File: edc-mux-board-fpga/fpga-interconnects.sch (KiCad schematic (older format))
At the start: 20 parts, among them J5 FPGA_JTAG, U6 10CL040YF484I7G, U63 S25FL128L

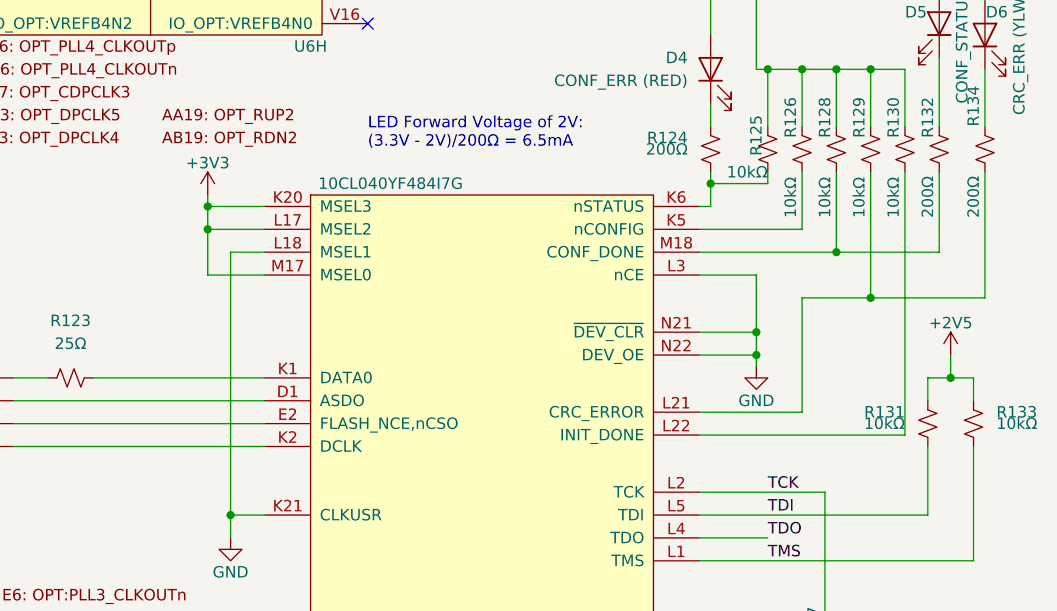
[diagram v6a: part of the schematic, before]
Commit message: Added labels to nets
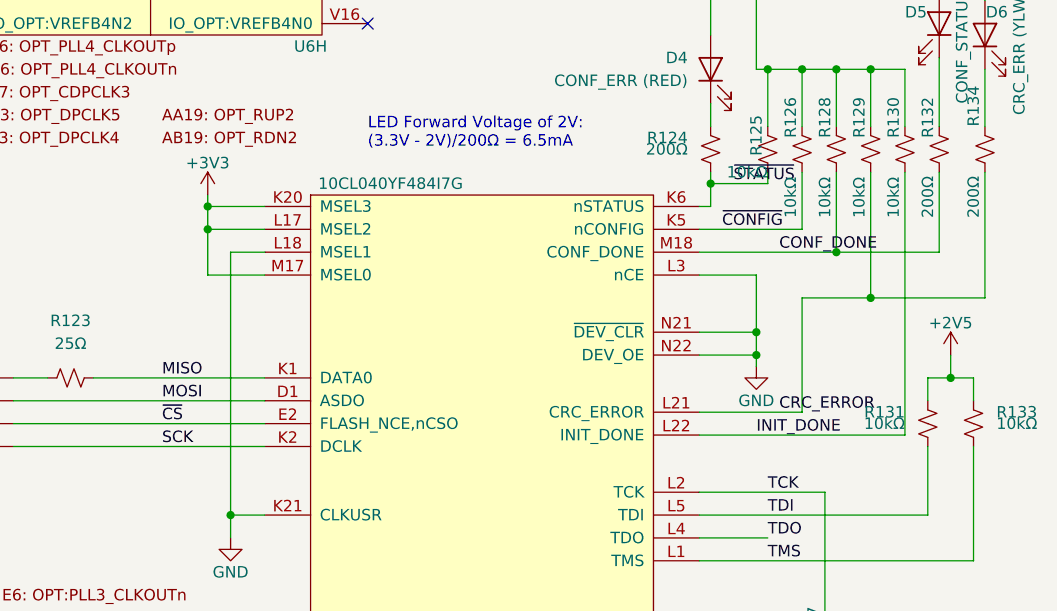
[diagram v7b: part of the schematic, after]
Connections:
- net MOSI: now reaches U6.D1 (ASDO), U63.5 (MOSI)
- net ~CS: now reaches U6.E2 (FLASH_NCE,nCSO), U63.1 (~CS)
- net MISO: now reaches R123.1, U6.K1 (DATA0)
- net SCK: now reaches U6.K2 (DCLK), U63.6 (SCK)
- net ~CONFIG: now reaches R126.1, U6.K5 (nCONFIG)
- net ~STATUS: now reaches R124.1, R125.1, U6.K6 (nSTATUS)
- net CRC_ERROR: now reaches R129.1, R134.2, U6.L21 (CRC_ERROR)
- net INIT_DONE: now reaches R130.1, U6.L22 (INIT_DONE)
- net CONF_DONE: now reaches R128.1, R132.1, U6.M18 (CONF_DONE)
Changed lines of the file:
@@
 Wire Bus Line
 	7100 1450 7100 3500
+Text Label 15250 5150 0    50   ~ 0
+INIT_DONE
+Text Label 15350 5050 0    50   ~ 0
+CRC_ERROR
+Text Label 15350 4350 0    50   ~ 0
+CONF_DONE
+Text Label 15100 4250 0    50   ~ 0
+~CONFIG
+Text Label 15150 4050 0    50   ~ 0
+~STATUS
+Text Label 12650 4900 0    50   ~ 0
+MISO
+Text Label 12650 5000 0    50   ~ 0
+MOSI
+Text Label 12650 5100 0    50   ~ 0
+~CS
+Text Label 12650 5200 0    50   ~ 0
+SCK
 $EndSCHEMATC

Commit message: updating FPGA pin assignments in schematic
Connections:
- wire segments 221 -> 234
- no-connect marks 203 -> 201
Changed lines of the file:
@@
 $Descr USLedger 17000 11000
 encoding utf-8
-Sheet 24 28
+Sheet 28 28
 Title ""
 Date ""
@@
 	1    0    0    -1
 $EndComp
+Text Label 8000 3100 2    50   ~ 0
+BCLK0
+Text Label 8000 3300 2    50   ~ 0
+WCLK0
 Text Label 8000 3000 2    50   ~ 0
-BCLK0
-Text Label 8000 2900 2    50   ~ 0
-WCLK0
-Text Label 8000 3300 2    50   ~ 0
 DOUT0
-Text Label 8000 3100 2    50   ~ 0
-DIN0
+Text Label 10150 1900 0    50   ~ 0
+BCLK1
+Text Label 10150 2000 0    50   ~ 0
+WCLK1
 Text Label 10150 1400 0    50   ~ 0
-BCLK1
+DOUT1
 Text Label 10150 1300 0    50   ~ 0
-WCLK1
-Text Label 10150 2000 0    50   ~ 0
-DOUT1
-Text Label 10150 1900 0    50   ~ 0
 DIN1
-Text Label 11500 1950 2    50   ~ 0
-BCLK4
-Text Label 10150 2100 0    50   ~ 0
+Text Label 10150 2800 0    50   ~ 0
 WCLK2
 Text Label 11500 1350 2    50   ~ 0
@@
 Text Label 11500 1250 2    50   ~ 0
 DIN3
-Text Label 1850 5350 2    50   ~ 0
-BCLK3
-Text Label 1850 5450 2    50   ~ 0
-WCLK3
 $Comp
 L SW-Intel:10CL040YF484I7G U?
@@
 	1    0    0    -1
 $EndComp
+Text Label 10150 2700 0    50   ~ 0
+BCLK2
 Text Label 10150 2200 0    50   ~ 0
-BCLK2
-Text Label 11500 1850 2    50   ~ 0
-WCLK4
-Text Label 10150 2800 0    50   ~ 0
 DOUT2
-Text Label 10150 2700 0    50   ~ 0
+Text Label 10150 2100 0    50   ~ 0
 DIN2
 $Comp
@@
 NoConn ~ 10050 2600
 NoConn ~ 10050 3300
-Wire Wire Line
-	1850 5350 2250 5350
-Wire Wire Line
-	1850 5450 2250 5450
+Text Label 13700 1450 0    50   ~ 0
+WCLK5
+Text Label 11500 1850 2    50   ~ 0
+DIN4
 Text Label 13700 1150 0    50   ~ 0
-WCLK5
-Text Label 11500 2250 2    50   ~ 0
-DIN4
-Text Label 13700 1350 0    50   ~ 0
 DIN5
-Text Label 11500 2350 2    50   ~ 0
+Text Label 11500 1950 2    50   ~ 0
 DOUT4
-Text Label 13700 1450 0    50   ~ 0
+Text Label 13700 1250 0    50   ~ 0
 DOUT5
 Text Label 11500 1650 2    50   ~ 0
@@
 Text Label 11500 3050 2    50   ~ 0
 DEV_ATT5
-Text Label 13700 1250 0    50   ~ 0
+Text Label 13700 1350 0    50   ~ 0
 BCLK5
 Wire Wire Line
@@
 Wire Wire Line
 	11500 1650 11650 1650
-Wire Wire Line
-	11500 1850 11650 1850
-Wire Wire Line
-	11500 1950 11650 1950
 Wire Wire Line
 	11500 2250 11650 2250
@@
 	13550 1550 13700 1550
 NoConn ~ 11650 1150
-NoConn ~ 11650 1450
-NoConn ~ 11650 1550
 NoConn ~ 11650 1750
 NoConn ~ 11650 2050
@@
 NoConn ~ 13550 2850
 NoConn ~ 13550 3350
+Text Label 3200 7450 0    50   ~ 0
+BCLK6
+Text Label 3200 7650 0    50   ~ 0
+WCLK6
 Text Label 3200 7850 0    50   ~ 0
-BCLK6
+DOUT6
 Text Label 3200 7750 0    50   ~ 0
-WCLK6
-Text Label 3200 7650 0    50   ~ 0
-DOUT6
-Text Label 3200 7450 0    50   ~ 0
 DIN6
 Text Label 3200 7150 0    50   ~ 0
@@
 Text Label 3200 7050 0    50   ~ 0
 DEV_ATT6
+Text Label 1000 8250 2    50   ~ 0
+WCLK7
 Text Label 3200 6650 0    50   ~ 0
-WCLK7
-Text Label 1000 8050 2    50   ~ 0
 DIN7
-Text Label 1000 8250 2    50   ~ 0
+Text Label 3200 6750 0    50   ~ 0
 DOUT7
 Text Label 1850 4850 2    50   ~ 0
@@
 Wire Wire Line
 	1850 4850 2250 4850
-Text Label 3200 6750 0    50   ~ 0
+Text Label 1000 8050 2    50   ~ 0
 BCLK7
 Wire Wire Line
+	3050 7450 3200 7450
+Wire Wire Line
+	3050 7650 3200 7650
+Wire Wire Line
+	3050 6650 3200 6650
+Wire Wire Line
+	3050 6750 3200 6750
+Wire Wire Line
+	3050 7050 3200 7050
+Wire Wire Line
+	3050 7150 3200 7150
+Wire Wire Line
 	1000 8050 1150 8050
 Wire Wire Line
 	1000 8250 1150 8250
-Wire Wire Line
-	3050 6650 3200 6650
-Wire Wire Line
-	3050 6750 3200 6750
-Wire Wire Line
-	3050 7050 3200 7050
-Wire Wire Line
-	3050 7150 3200 7150
-Wire Wire Line
-	3050 7450 3200 7450
-Wire Wire Line
-	3050 7650 3200 7650
 Wire Wire Line
 	3050 7750 3200 7750
@@
 Text Label 4250 7550 2    50   ~ 0
 BCLK9
+Text Label 6450 6950 0    50   ~ 0
+DOUT8
+Text Label 6450 6750 0    50   ~ 0
+DIN8
 Text Label 6450 6450 0    50   ~ 0
-DOUT8
+DEV_INT8
 Text Label 6450 6350 0    50   ~ 0
-DIN8
-Text Label 4250 8050 2    50   ~ 0
-DEV_INT8
-Text Label 4250 7950 2    50   ~ 0
 DEV_ATT8
 NoConn ~ 1150 6350
@@
 Text Label 4250 7650 2    50   ~ 0
 WCLK9
-Text Label 4250 6850 2    50   ~ 0
+Text Label 4250 7950 2    50   ~ 0
 DIN9
-Text Label 4250 7050 2    50   ~ 0
+Text Label 4250 8050 2    50   ~ 0
 DOUT9
-Text Label 4250 6750 2    50   ~ 0
-DEV_INT9
-Text Label 4250 6650 2    50   ~ 0
-DEV_ATT9
-Wire Wire Line
-	4250 6650 4400 6650
-Wire Wire Line
-	4250 6750 4400 6750
 Wire Wire Line
 	4250 6850 4400 6850
@@
 	4250 7050 4400 7050
 Wire Wire Line
+	4250 7950 4400 7950
+Wire Wire Line
+	4250 8050 4400 8050
+Wire Wire Line
 	4250 7550 4400 7550
 Wire Wire Line
 	4250 7650 4400 7650
 Wire Wire Line
-	4250 7950 4400 7950
-Wire Wire Line
-	4250 8050 4400 8050
-Wire Wire Line
-	6300 6350 6450 6350
-Wire Wire Line
-	6300 6450 6450 6450
+	6450 6350 6300 6350
+Wire Wire Line
+	6450 6450 6300 6450
+Wire Wire Line
+	6300 6750 6450 6750
+Wire Wire Line
+	6300 6950 6450 6950
 $Comp
 L SW-Intel:10CL040YF484I7G U6
@@
 NoConn ~ 6300 6550
 NoConn ~ 6300 6650
-NoConn ~ 6300 6750
-NoConn ~ 6300 6950
 NoConn ~ 6300 7050
 NoConn ~ 6300 7150
 NoConn ~ 6300 7250
 NoConn ~ 6300 8450
+Text Label 7350 7050 2    50   ~ 0
+BCLK10
+Text Label 7350 7250 2    50   ~ 0
+WCLK10
 Text Label 7350 7650 2    50   ~ 0
-BCLK10
+DOUT10
 Text Label 7350 7550 2    50   ~ 0
-WCLK10
-Text Label 7350 7250 2    50   ~ 0
-DOUT10
-Text Label 7350 7050 2    50   ~ 0
 DIN10
 Text Label 9550 6550 0    50   ~ 0
@@
 Text Label 9550 6750 0    50   ~ 0
 DEV_ATT10
+Text Label 7350 6550 2    50   ~ 0
+WCLK11
 Text Label 7350 6650 2    50   ~ 0
-WCLK11
-Text Label 7350 6450 2    50   ~ 0
 DIN11
-Text Label 7350 6550 2    50   ~ 0
+Text Label 7350 6750 2    50   ~ 0
 DOUT11
 Text Label 9550 6650 0    50   ~ 0
@@
 Text Label 9550 7650 0    50   ~ 0
 DEV_ATT11
-Text Label 7350 6750 2    50   ~ 0
+Text Label 7350 6450 2    50   ~ 0
 BCLK11
 Wire Wire Line
 	7350 6450 7500 6450
+Text Label 13100 7400 0    50   ~ 0
+BCLK12
+Text Label 13100 7500 0    50   ~ 0
+WCLK12
 Text Label 13100 7700 0    50   ~ 0
-BCLK12
+DOUT12
 Text Label 13100 7600 0    50   ~ 0
-WCLK12
-Text Label 13100 7500 0    50   ~ 0
-DOUT12
-Text Label 13100 7400 0    50   ~ 0
 DIN12
 Text Label 10800 8000 2    50   ~ 0
@@
 NoConn ~ 9400 8150
 NoConn ~ 9400 8250
+Text Label 13100 6900 0    50   ~ 0
+WCLK13
+Text Label 10800 8200 2    50   ~ 0
+WCLK14
+Text Label 10800 7200 2    50   ~ 0
+WCLK15
 Text Label 13100 7000 0    50   ~ 0
-WCLK13
+DIN13
 Text Label 13100 6600 0    50   ~ 0
-WCLK14
+DIN14
 Text Label 10800 7500 2    50   ~ 0
-WCLK15
-Text Label 13100 6800 0    50   ~ 0
-DIN13
-Text Label 10800 8300 2    50   ~ 0
-DIN14
-Text Label 10800 7100 2    50   ~ 0
 DIN15
-Text Label 13100 6900 0    50   ~ 0
+Text Label 13100 7200 0    50   ~ 0
 DOUT13
-Text Label 10800 8200 2    50   ~ 0
+Text Label 13100 6700 0    50   ~ 0
 DOUT14
-Text Label 10800 7200 2    50   ~ 0
+Text Label 10800 7700 2    50   ~ 0
 DOUT15
 Text Label 10800 6500 2    50   ~ 0
@@
 Text Label 10800 6700 2    50   ~ 0
 DEV_ATT15
-Text Label 13100 7200 0    50   ~ 0
+Text Label 13100 6800 0    50   ~ 0
 BCLK13
-Text Label 13100 6700 0    50   ~ 0
+Text Label 10800 8300 2    50   ~ 0
 BCLK14
-Text Label 10800 7700 2    50   ~ 0
+Text Label 10800 7100 2    50   ~ 0
 BCLK15
 Wire Wire Line
@@
 Text Label 12650 5200 0    50   ~ 0
 SCK
+Wire Wire Line
+	15250 2500 15250 3400
+Wire Wire Line
+	15000 4150 15300 4150
+Wire Wire Line
+	15750 3850 15750 4450
+Wire Wire Line
+	15900 4550 16000 4550
+Connection ~ 15900 4550
+Wire Wire Line
+	15900 4550 15900 3850
+Wire Wire Line
+	15750 4450 16000 4450
+Connection ~ 15750 4450
+Wire Wire Line
+	15750 4450 15750 5050
+Wire Wire Line
+	15600 4350 16000 4350
+Connection ~ 15600 4350
+Connection ~ 15300 4150
+Wire Wire Line
+	15300 4150 16000 4150
+Wire Wire Line
+	11500 1950 11650 1950
+Wire Wire Line
+	11500 1850 11650 1850
+Text Label 11500 2350 2    50   ~ 0
+WCLK4
+Text Label 11500 2250 2    50   ~ 0
+BCLK4
+Wire Wire Line
+	2250 5350 2100 5350
+Connection ~ 2100 5350
+Wire Wire Line
+	2100 5350 2100 5250
+Wire Wire Line
+	2250 5450 2100 5450
+Connection ~ 2100 5450
+Wire Wire Line
+	2100 5450 2100 5350
+Text Label 11500 1450 2    50   ~ 0
+BCLK3
+Text Label 11500 1550 2    50   ~ 0
+WCLK3
+Wire Wire Line
+	11500 1450 11650 1450
+Wire Wire Line
+	11500 1550 11650 1550
+Text Label 8000 2900 2    50   ~ 0
+DIN0
+Text Label 4250 7050 2    50   ~ 0
+DEV_INT9
+Text Label 4250 6850 2    50   ~ 0
+DEV_ATT9
+NoConn ~ 4400 6650
+NoConn ~ 4400 6750
+Wire Bus Line
+	7100 1450 7100 3500
 $EndSCHEMATC
